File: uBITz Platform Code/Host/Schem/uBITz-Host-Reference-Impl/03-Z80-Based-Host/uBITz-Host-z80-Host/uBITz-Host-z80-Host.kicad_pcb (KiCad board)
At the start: 2 copper layers, 6 parts, among them U1 Z084000xP, U2 ATF1504AS-10AU44, U3 24LC16BT-I_SN, U4 SN74LS612N, Y1 ACH-14.31818MHZ-EK

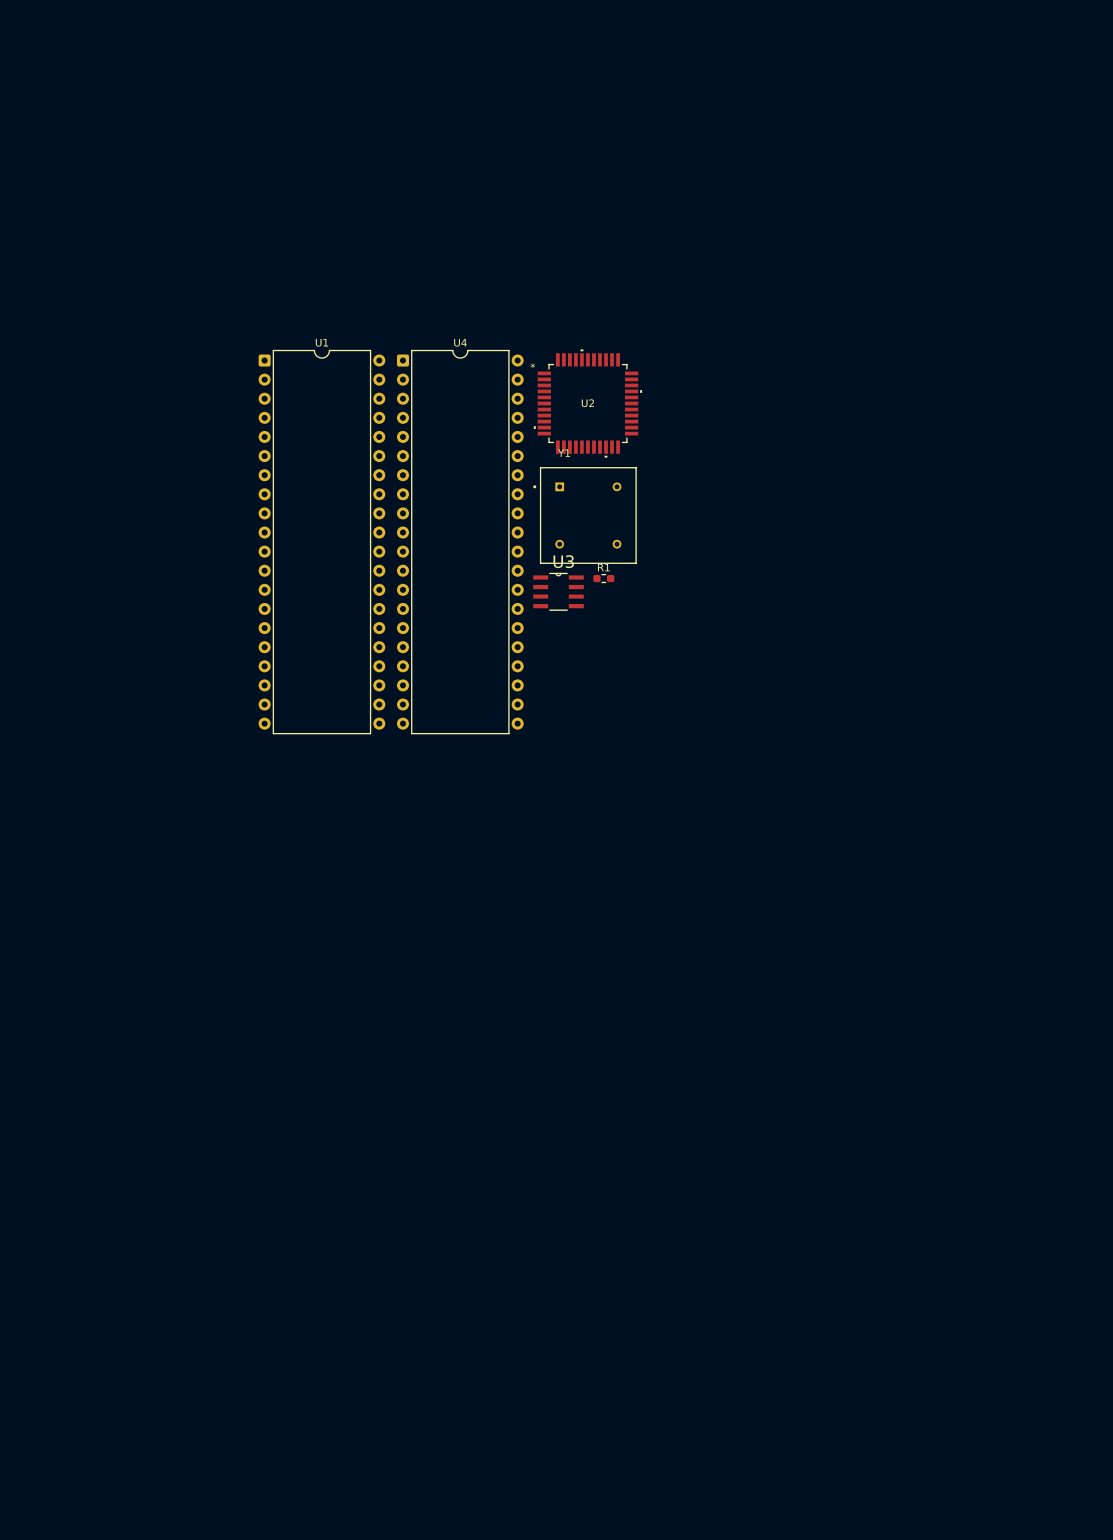
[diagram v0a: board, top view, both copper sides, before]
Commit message: Removed the Serial Profile and first commit of the a Host
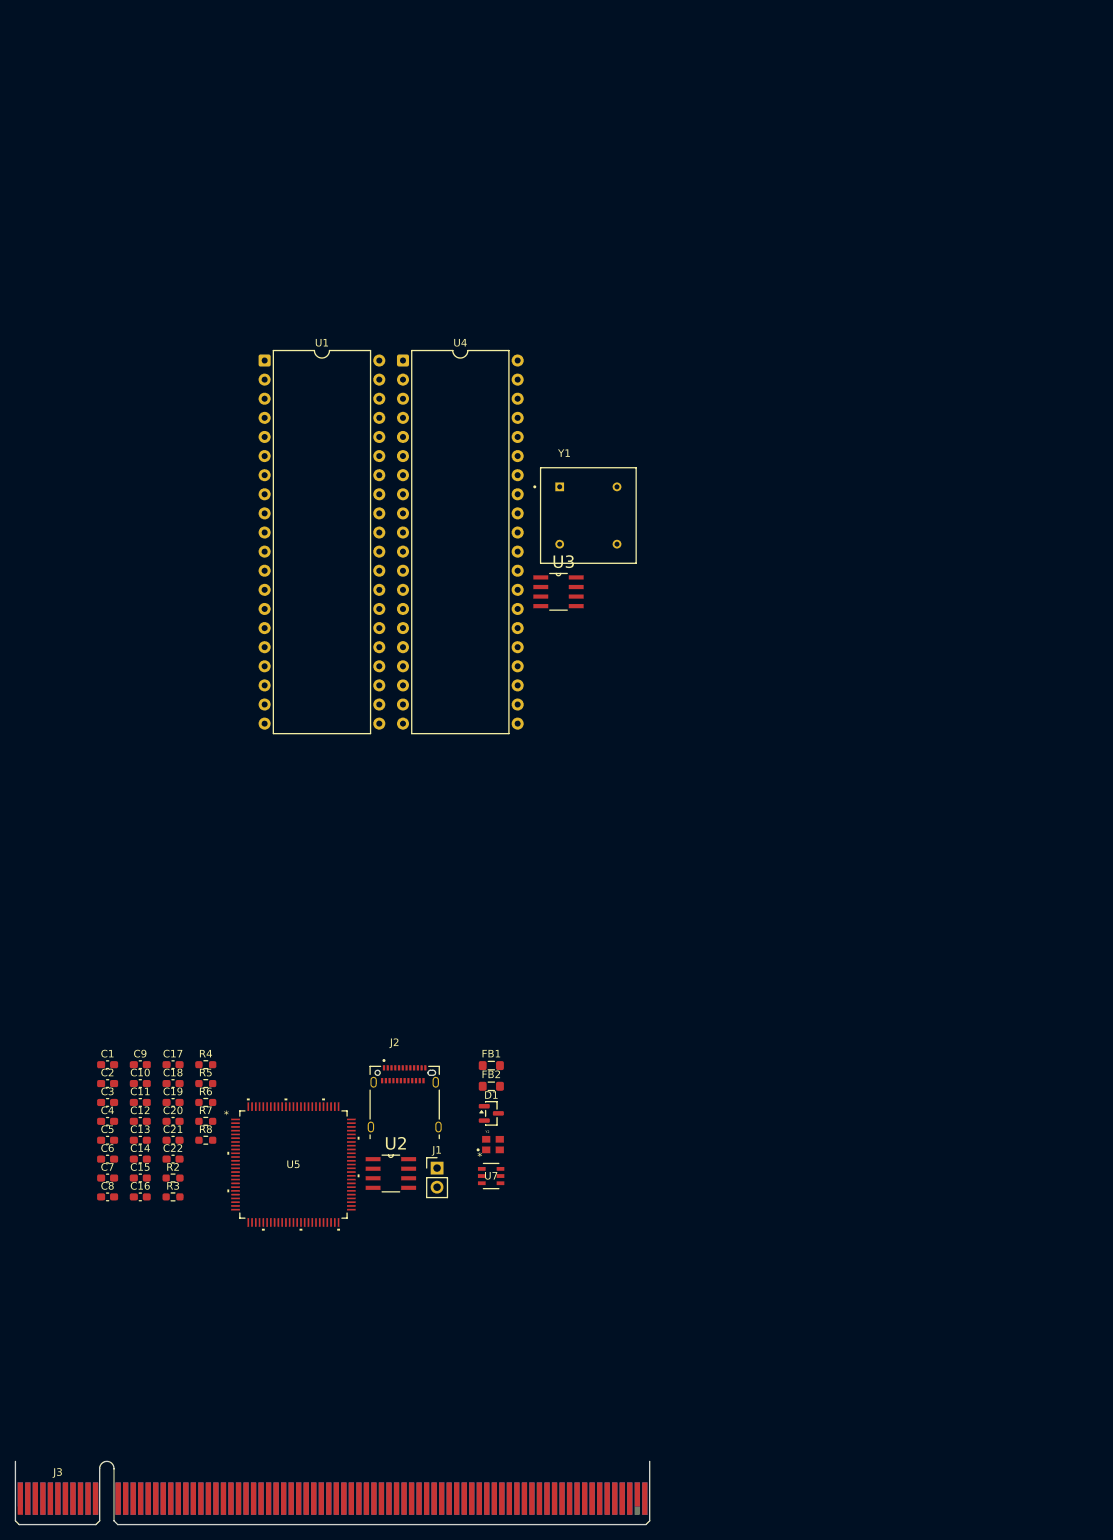
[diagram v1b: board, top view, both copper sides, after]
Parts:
- removed R1: 1k, Resistor_SMD:R_0603_1608Metric_Pad0.98x0.95mm_HandSolder
- added C1: 1u, Capacitor_SMD:C_0603_1608Metric_Pad1.08x0.95mm_HandSolder, F.Cu at (42.8, 189.5)
- added C10: 1000n, Capacitor_SMD:C_0603_1608Metric_Pad1.08x0.95mm_HandSolder, F.Cu at (47.1, 192.0)
- added C11: 1000n, Capacitor_SMD:C_0603_1608Metric_Pad1.08x0.95mm_HandSolder, F.Cu at (47.1, 194.6)
- added C12: 100n, Capacitor_SMD:C_0603_1608Metric_Pad1.08x0.95mm_HandSolder, F.Cu at (47.1, 197.1)
- added C13: 100n, Capacitor_SMD:C_0603_1608Metric_Pad1.08x0.95mm_HandSolder, F.Cu at (47.1, 199.6)
- added C14: 100n, Capacitor_SMD:C_0603_1608Metric_Pad1.08x0.95mm_HandSolder, F.Cu at (47.1, 202.1)
- added C15: 100n, Capacitor_SMD:C_0603_1608Metric_Pad1.08x0.95mm_HandSolder, F.Cu at (47.1, 204.6)
- added C16: 100n, Capacitor_SMD:C_0603_1608Metric_Pad1.08x0.95mm_HandSolder, F.Cu at (47.1, 207.1)
- added C17: 100n, Capacitor_SMD:C_0603_1608Metric_Pad1.08x0.95mm_HandSolder, F.Cu at (51.5, 189.5)
- added C18: 100n, Capacitor_SMD:C_0603_1608Metric_Pad1.08x0.95mm_HandSolder, F.Cu at (51.5, 192.0)
- added C19: 100n, Capacitor_SMD:C_0603_1608Metric_Pad1.08x0.95mm_HandSolder, F.Cu at (51.5, 194.6)
- added C2: 220n, Capacitor_SMD:C_0603_1608Metric_Pad1.08x0.95mm_HandSolder, F.Cu at (42.8, 192.0)
- added C20: 10u, Capacitor_SMD:C_0603_1608Metric_Pad1.08x0.95mm_HandSolder, F.Cu at (51.5, 197.1)
- added C21: 100n, Capacitor_SMD:C_0603_1608Metric_Pad1.08x0.95mm_HandSolder, F.Cu at (51.5, 199.6)
- added C22: 100n, Capacitor_SMD:C_0603_1608Metric_Pad1.08x0.95mm_HandSolder, F.Cu at (51.5, 202.1)
- added C3: 220n, Capacitor_SMD:C_0603_1608Metric_Pad1.08x0.95mm_HandSolder, F.Cu at (42.8, 194.6)
- added C4: 2u, Capacitor_SMD:C_0603_1608Metric_Pad1.08x0.95mm_HandSolder, F.Cu at (42.8, 197.1)
- added C5: 10u, Capacitor_SMD:C_0603_1608Metric_Pad1.08x0.95mm_HandSolder, F.Cu at (42.8, 199.6)
- added C6: 10u, Capacitor_SMD:C_0603_1608Metric_Pad1.08x0.95mm_HandSolder, F.Cu at (42.8, 202.1)
- added C7: 10u, Capacitor_SMD:C_0603_1608Metric_Pad1.08x0.95mm_HandSolder, F.Cu at (42.8, 204.6)
- added C8: 1000n, Capacitor_SMD:C_0603_1608Metric_Pad1.08x0.95mm_HandSolder, F.Cu at (42.8, 207.1)
- added C9: 1000n, Capacitor_SMD:C_0603_1608Metric_Pad1.08x0.95mm_HandSolder, F.Cu at (47.1, 189.5)
- added D1: BAT54C, Package_TO_SOT_SMD:SOT-23, F.Cu at (93.8, 196.0)
- added FB1: 600R/500mA, Inductor_SMD:L_0805_2012Metric_Pad1.05x1.20mm_HandSolder, F.Cu at (93.8, 189.7)
- added FB2: 600R/500mA, Inductor_SMD:L_0805_2012Metric_Pad1.05x1.20mm_HandSolder, F.Cu at (93.8, 192.4)
- added J1: Conn_01x02_Pin, Connector_PinHeader_2.54mm:PinHeader_1x02_P2.54mm_Vertical, F.Cu at (86.6, 203.3)
- added J2: 12401610E4_2A, Footprints:AMPHENOL_12401610E4_2A, F.Cu at (82.3, 195.0)
- added J3: ~, Connector_PCBEdge:BUS_PCIexpress_x16, F.Cu at (31.2, 247.2)
- added R2: 2k2, Resistor_SMD:R_0603_1608Metric_Pad0.98x0.95mm_HandSolder, F.Cu at (51.5, 204.6)
- added R3: 2k2, Resistor_SMD:R_0603_1608Metric_Pad0.98x0.95mm_HandSolder, F.Cu at (51.5, 207.1)
- added R4: 5k1, Resistor_SMD:R_0603_1608Metric_Pad0.98x0.95mm_HandSolder, F.Cu at (55.9, 189.5)
- added R5: 5k1, Resistor_SMD:R_0603_1608Metric_Pad0.98x0.95mm_HandSolder, F.Cu at (55.9, 192.0)
- added R6: 12k, Resistor_SMD:R_0603_1608Metric_Pad0.98x0.95mm_HandSolder, F.Cu at (55.9, 194.6)
- added R7: 12k, Resistor_SMD:R_0603_1608Metric_Pad0.98x0.95mm_HandSolder, F.Cu at (55.9, 197.1)
- added R8: 2k2, Resistor_SMD:R_0603_1608Metric_Pad0.98x0.95mm_HandSolder, F.Cu at (55.9, 199.6)
- added U5: ATF1504AS-10AU100, Footprints:100A_ATM-L, F.Cu at (67.5, 202.8)
- added U7: 93LC56BT-I/OT, Footprints:SOT-23-6_MC_MCH-L, F.Cu at (93.8, 204.3)
- added Y2: ECS-2033-120-BN, Footprints:OSC_ECS-2033-120-BN, F.Cu at (94.0, 200.2)
- U2: value ATF1504AS-10AU44 -> MAX662ACSA_T; footprint Footprints:44A_ATM-M -> Footprints:SOIC127P600X175-8N
- moved U2 105.6 mm to (80.4, 204.0)
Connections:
- U2 pad 1: /TDI -> Net-(U2-C1-)
- U2 pad 2: /CPUCLK -> Net-(U2-C1+)
- U2 pad 3: /~{DOCK_MREQ} -> Net-(U2-C2-)
- U2 pad 4: GND -> Net-(U2-C2+)
- U2 pad 5: /A0 -> +5V_VBUS
- U2 pad 6: /A1 -> +12V
- U2 pad 7: /TMS -> GND
- U2 pad 8: /A2 -> GND
- U3 pad 1: unconnected-(U3-A0-Pad1) -> GND
- U3 pad 2: unconnected-(U3-A1-Pad2) -> GND
- U3 pad 3: unconnected-(U3-A2-Pad3) -> GND
- U3 pad 4: unconnected-(U3-VSS-Pad4) -> GND
- U3 pad 5: unconnected-(U3-SDA-Pad5) -> /BUS_SDA
- U3 pad 6: unconnected-(U3-SCL-Pad6) -> /BUS_SCL
- U3 pad 7: unconnected-(U3-WP-Pad7) -> GND
- U3 pad 8: unconnected-(U3-VCC-Pad8) -> +5V
- U4 pad 1: /RS2 -> /B_RS2
- U4 pad 13: /~{MM} -> /B_~{MM}
- U4 pad 14: /A12 -> /A16
- U4 pad 15: /A13 -> /A17
- U4 pad 16: /A14 -> /A18
- U4 pad 17: /A15 -> /A19
- U4 pad 18: /A16 -> /A20
- U4 pad 19: /A17 -> /A21
- U4 pad 22: /A18 -> /A22
- U4 pad 23: /A19 -> /A23
- U4 pad 24: /A20 -> /A12
- U4 pad 25: /A21 -> /A13
- U4 pad 26: /A22 -> /A14
- U4 pad 27: /A23 -> /A15
- U4 pad 3: /RS3 -> /B_RS3
- U4 pad 31: GND -> /B_D8
- U4 pad 32: GND -> /B_D9
- U4 pad 33: GND -> /B_D10
- U4 pad 34: GND -> /B_D11
- U4 pad 36: /RS0 -> /B_RS0
- U4 pad 38: /RS1 -> /B_RS1
- U4 pad 4: /~{CS} -> /B_~{CS}
- U4 pad 5: /~{STROBE} -> /B_~{STROBE}
- U4 pad 6: /R/~{W} -> GND
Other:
- board outline added: 84.3 x 8.4 mm

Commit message: Committing the first fully completed version of the Z80 based host
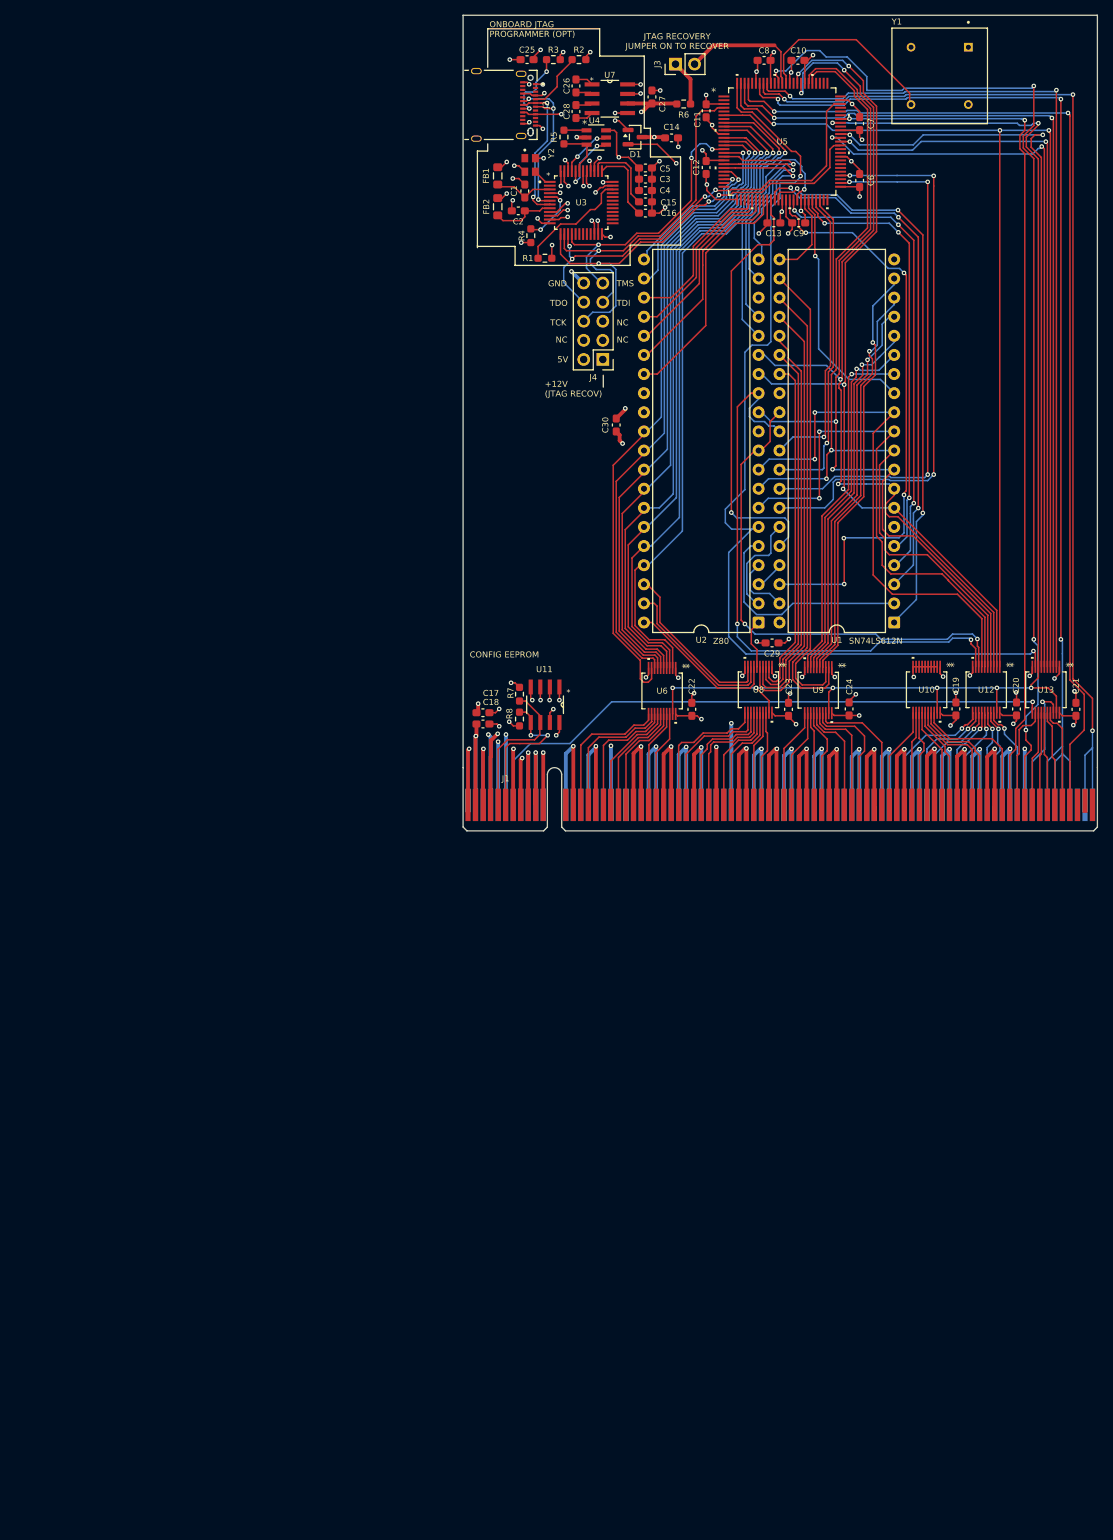
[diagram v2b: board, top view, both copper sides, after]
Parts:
- removed the J3 at (31.2, 247.2)
- added C19: 100n, Capacitor_SMD:C_0603_1608Metric_Pad1.08x0.95mm_HandSolder, F.Cu at (155.6, 142.2)
- added C20: 100n, Capacitor_SMD:C_0603_1608Metric_Pad1.08x0.95mm_HandSolder, F.Cu at (163.6, 142.2)
- added C21: 100n, Capacitor_SMD:C_0603_1608Metric_Pad1.08x0.95mm_HandSolder, F.Cu at (171.5, 142.3)
- added C22: 100n, Capacitor_SMD:C_0603_1608Metric_Pad1.08x0.95mm_HandSolder, F.Cu at (120.5, 142.3)
- added C23: 100n, Capacitor_SMD:C_0603_1608Metric_Pad1.08x0.95mm_HandSolder, F.Cu at (133.3, 142.3)
- added C24: 100n, Capacitor_SMD:C_0603_1608Metric_Pad1.08x0.95mm_HandSolder, F.Cu at (141.3, 142.2)
- added C29: 100n, Capacitor_SMD:C_0603_1608Metric_Pad1.08x0.95mm_HandSolder, F.Cu at (131.1, 133.5)
- added C30: 100n, Capacitor_SMD:C_0603_1608Metric_Pad1.08x0.95mm_HandSolder, F.Cu at (110.4, 104.5)
- added J1: ~, Connector_PCBEdge:BUS_PCIexpress_x16, F.Cu at (90.7, 155.0)
- added J4: Conn_02x05_Top_Bottom, Connector_PinHeader_2.54mm:PinHeader_2x05_P2.54mm_Vertical, F.Cu at (108.6, 95.8)
- added R6: 2k2, Resistor_SMD:R_0603_1608Metric_Pad0.98x0.95mm_HandSolder, F.Cu at (119.4, 61.9)
- added U10: SN74LVC245ADGVR, Footprints:DGV20-M, F.Cu at (151.7, 139.7)
- added U12: SN74LVC245ADGVR, Footprints:DGV20-M, F.Cu at (159.6, 139.7)
- added U13: SN74LVC245ADGVR, Footprints:DGV20-M, F.Cu at (167.5, 139.7)
- added U3: FT232HL, Footprints:QFP50P900X900X160-48N, F.Cu at (105.8, 75.0)
- added U6: SN74LVC245ADGVR, Footprints:DGV20-M, F.Cu at (116.5, 139.9)
- added U8: SN74LVC245ADGVR, Footprints:DGV20-M, F.Cu at (129.3, 139.7)
- added U9: SN74LVC245ADGVR, Footprints:DGV20-M, F.Cu at (137.2, 139.8)
- C17: renamed from C21; value 100n -> 10u
- C18: renamed from C22; value 100n -> 10u
- U4: renamed from U7; footprint Footprints:SOT-23-6_MC_MCH-L -> Footprints:SOT-23-6_MC_MCH
- U5: footprint Footprints:100A_ATM-L -> Footprints:100A_ATM
- moved C10 174.5 mm to (134.6, 56.0), turned to 180 degrees
- moved C8 167.9 mm to (130.1, 56.0), turned to 180 degrees
- moved C7 165.5 mm to (142.8, 64.5), turned to 90 degrees
- moved C6 157.4 mm to (142.8, 72.0), turned to 90 degrees
- moved C9 154.2 mm to (134.7, 77.7)
- moved C25 151.7 mm to (98.5, 56.0), turned to 180 degrees
- moved C4 151.7 mm to (114.3, 73.3)
- moved C3 150.8 mm to (114.3, 71.8)
- moved U5 150.7 mm to (132.5, 66.8)
- moved J3 150.1 mm to (118.3, 56.5), turned to 90 degrees
- moved C27 147.6 mm to (115.2, 60.9), turned to 90 degrees
- moved C14 146.5 mm to (117.8, 66.3)
- moved C26 146.5 mm to (105.0, 59.5), turned to 90 degrees
- moved U7 145.8 mm to (109.5, 61.1)
- moved C28 145.7 mm to (105.0, 62.9), turned to 90 degrees
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- renumbered C6 to C1, C16 to C10, C17 to C11, C18 to C12, C19 to C13, C20 to C14, C10 to C15, C11 to C16, C5 to C2, C4 to C25, C2 to C26, C1 to C27, C3 to C28, C7 to C3, C8 to C4, C9 to C5, C12 to C6, C13 to C7, C14 to C8, C15 to C9, J1 to J3, R6 to R1, R4 to R2, R5 to R3, R7 to R4, R8 to R5, R3 to R7, R2 to R8, U4 to U1, U3 to U11, U1 to U2, U2 to U7
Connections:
- net /B_RS0 renamed /MAP_RS0
- net /B_RS2 renamed /MAP_RS2
- net /DM renamed /D-
- net /DP renamed /D+
- J3 pad 2: GND -> /RECOV
- R1 pad 2: GND -> VCCD
- U1 pad 13: /B_~{MM} -> /MAP_~{MM}
- U1 pad 21: GND -> /MAP_~{ME}
- U1 pad 3: /B_RS3 -> /MAP_RS3
- U1 pad 31: /B_D8 -> /MAP_D8
- U1 pad 32: /B_D9 -> /MAP_D9
- U1 pad 33: /B_D10 -> /MAP_D10
- U1 pad 34: /B_D11 -> /MAP_D11
- U1 pad 38: /B_RS1 -> /MAP_RS1
- U1 pad 4: /B_~{CS} -> /MAP_~{CS}
- U1 pad 5: /B_~{STROBE} -> /MAP_~{STROBE}
- U2 pad 23: unconnected-(U1-~{BUSACK}-Pad23) -> /~{BUSACK}
- U2 pad 25: +5V -> /~{BUSREQ}
- U5 pad 10: /A3 -> /A4
- U5 pad 12: /A4 -> /A3
- U5 pad 13: /A5 -> /A2
- U5 pad 14: /A6 -> /A1
- U5 pad 16: /A7 -> /A0
- U5 pad 17: /~{MREQ} -> /~{NMI}
- U5 pad 19: /~{IORQ} -> /~{MREQ}
- U5 pad 20: /~{RD} -> /~{IORQ}
- U5 pad 23: /~{INT} -> /~{RD}
- U5 pad 25: /~{NMI} -> unconnected-(U5-I/O-Pad25)
- U5 pad 29: /~{WAIT} -> /~{BUSACK}
- U5 pad 30: /~{RESET} -> /~{WAIT}
- U5 pad 31: /B_~{CS} -> /~{BUSREQ}
- U5 pad 32: GND -> /~{RESET}
- U5 pad 33: /B_~{STROBE} -> /~{M1}
- U5 pad 36: /B_RS1 -> /MAP_RS3
- U5 pad 40: /B_RS3 -> /MAP_RS1
- U5 pad 41: /~{M1} -> /MAP_~{CS}
- U5 pad 42: unconnected-(U5-I/O/PD2-Pad42) -> /~{INT}
- U5 pad 44: unconnected-(U5-I/O-Pad44) -> /MAP_~{ME}
- U5 pad 45: unconnected-(U5-I/O-Pad45) -> /MAP_~{MM}
- U5 pad 46: unconnected-(U5-I/O-Pad46) -> /MAP_~{STROBE}
- U5 pad 47: unconnected-(U5-I/O-Pad47) -> /MAP_D8
- U5 pad 48: unconnected-(U5-I/O-Pad48) -> /MAP_D9
- U5 pad 52: GND -> /MAP_D10
- U5 pad 54: GND -> /MAP_D11
- U5 pad 56: GND -> unconnected-(U5-I/O-Pad56)
- U5 pad 57: GND -> unconnected-(U5-I/O-Pad57)
- U5 pad 58: GND -> unconnected-(U5-I/O-Pad58)
- U5 pad 6: /A0 -> /A7
- U5 pad 60: GND -> unconnected-(U5-I/O-Pad60)
- U5 pad 61: GND -> unconnected-(U5-I/O-Pad61)
- U5 pad 63: GND -> /~{BUS_MEM1_CS}
- U5 pad 64: GND -> /~{BUS_MEM0_CS}
- U5 pad 65: GND -> /~{BUS_MREQ}
- U5 pad 67: GND -> unconnected-(U5-I/O-Pad67)
- U5 pad 68: GND -> /~{BUS_DMA_GNT}
- U5 pad 69: GND -> /~{BUS_DMA_REQ}
- U5 pad 71: /B_D11 -> unconnected-(U5-I/O-Pad71)
- U5 pad 75: /B_D10 -> unconnected-(U5-I/O-Pad75)
- U5 pad 76: /B_D9 -> unconnected-(U5-I/O-Pad76)
- U5 pad 79: /B_D8 -> unconnected-(U5-I/O-Pad79)
- U5 pad 8: /A1 -> /A6
- U5 pad 85: Net-(U5-INPUT/GCLR) -> unconnected-(U5-I/O/GCLK3-Pad85)
- U5 pad 88: GND -> /RECOV
- U5 pad 89: Net-(U5-INPUT/GCLR) -> /~{BUS_RESET}
- U5 pad 9: /A2 -> /A5
- U5 pad 90: Net-(U5-INPUT/GCLR) -> unconnected-(U5-INPUT/OE2/GCLK2-Pad90)
- U5 pad 96: /~{BUS_RESET} -> unconnected-(U5-I/O-Pad96)
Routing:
- net GND: track 0.00 -> 604.1 mm, vias 0 -> 96
- net /BUS_R/~{W}: track 0.00 -> 188.2 mm, vias 0 -> 3
- net /~{BUS_DMA_GNT}: track 0.00 -> 176.7 mm, vias 0 -> 8
- net /~{BUS_CPU_INT}: track 0.00 -> 160.0 mm, vias 0 -> 3
- net /~{BUS_CPU_NMI}: track 0.00 -> 146.7 mm, vias 0 -> 3
- net /~{BUS_READY}: track 0.00 -> 139.3 mm, vias 0 -> 2
- net /~{BUS_RESET}: track 0.00 -> 139.0 mm, vias 0 -> 4
- net /CPUCLK: track 0.00 -> 134.5 mm, vias 0 -> 2
- net /D1: track 0.00 -> 120.6 mm, vias 0 -> 4
- net /D3: track 0.00 -> 119.1 mm, vias 0 -> 2
- net /~{BUS_IORQ}: track 0.00 -> 117.8 mm, vias 0 -> 2
- net /~{BUS_DMA_REQ}: track 0.00 -> 117.5 mm, vias 0 -> 2
- net /~{BUS_CPU_ACK}: track 0.00 -> 117.1 mm, vias 0 -> 2
- net /D2: track 0.00 -> 115.6 mm, vias 0 -> 2
- net /D0: track 0.00 -> 115.3 mm, vias 0 -> 4
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- added copper zone on In2.Cu, net +3V3
- added copper zone on In2.Cu, net +5V
- added copper zone on In2.Cu, net +5V_CPLD
- added copper zone on In2.Cu, net +5V_VBUS
- added copper zone on In1.Cu, net GND
- added copper zone on In2.Cu, net VCCD
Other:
- board size 84.3 x 8.4 mm -> 84.3 x 100 mm
- copper layers 2 -> 4
- board text added: "*"
- board text added: "+12V (JTAG RECOV)"
- board text added: "5V"
- board text added: "CONFIG EEPROM"
- board text added: "GND"
- board text added: "JTAG RECOVERY JUMPER ON TO RECOVER"
- board text added: "NC"
- board text added: "ONBOARD JTAG PROGRAMMER (OPT)"
- board text added: "SN74LS612N"
- board text added: "TCK"
- board text added: "TDI"
- board text added: "TDO"
- board text added: "TMS"
- board text added: "Z80"
